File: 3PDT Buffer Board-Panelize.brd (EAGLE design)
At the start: 81.3 x 49.3 mm, 68 parts, among them Q1 J201, Q2 J201, Q3 J201, Q4 J201, SW1 3PDT, SW2 3PDT, SW3 3PDT, SW4 3PDT

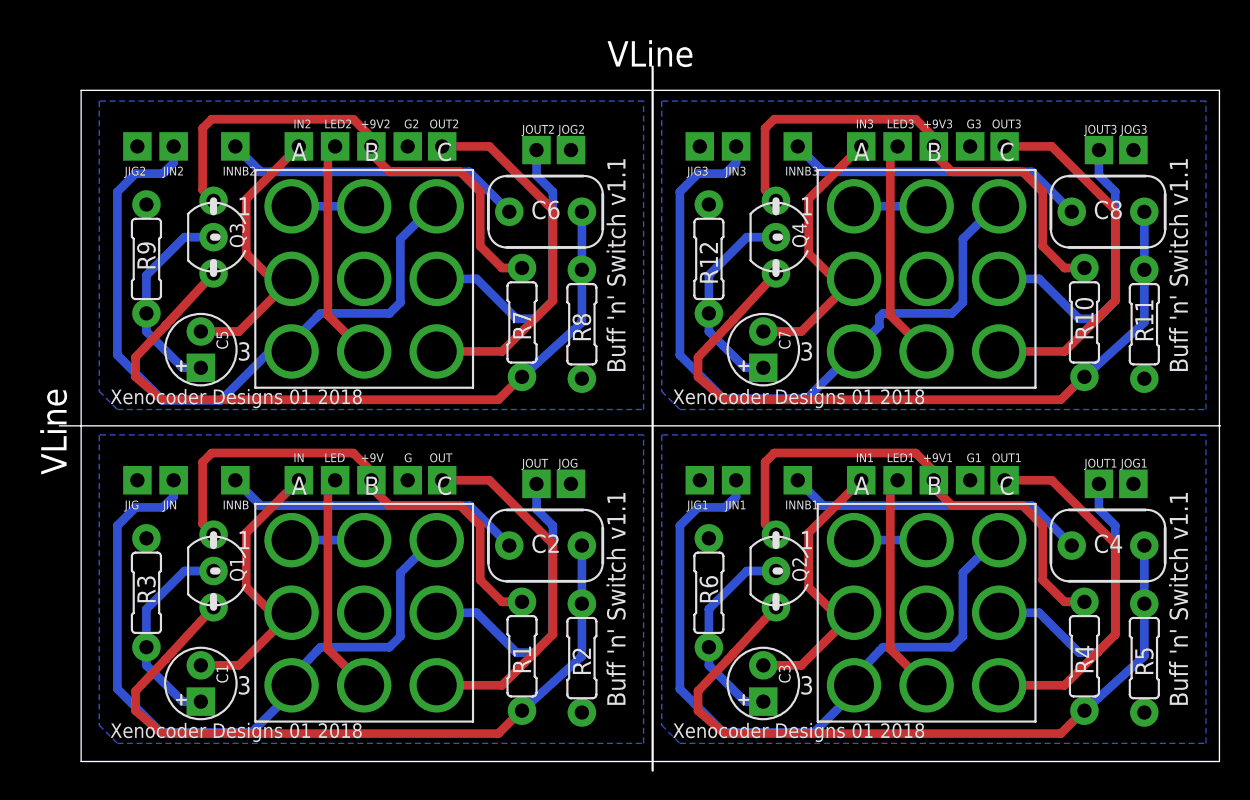
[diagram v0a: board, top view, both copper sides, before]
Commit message: Made first panelized board
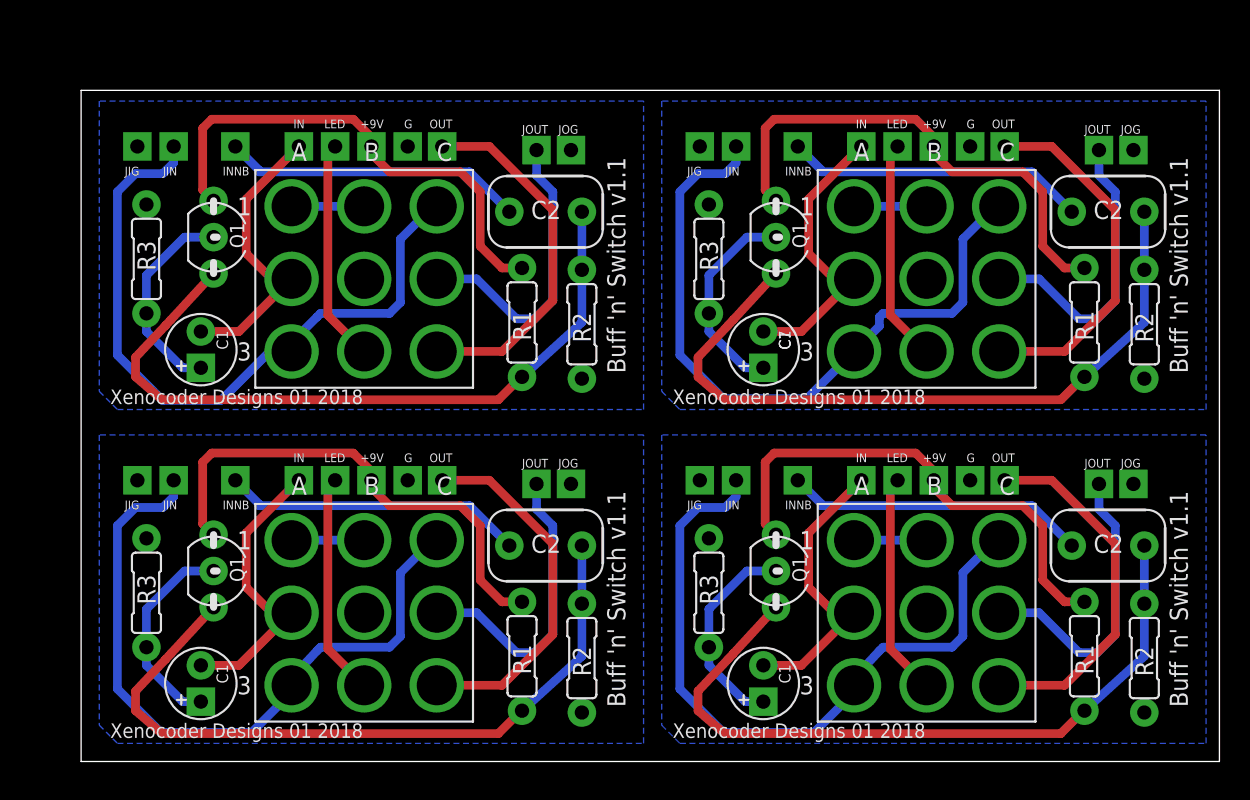
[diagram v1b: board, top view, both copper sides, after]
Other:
- board size 81.3 x 49.3 mm -> 79.7 x 47 mm
- board text removed: "VLine"
